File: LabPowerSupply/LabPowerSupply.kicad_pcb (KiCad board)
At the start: 4 copper layers, 213 parts, among them Q1_CP1 FMMT495TA, Q1_CP2 FMMT495TA, Q1_LVR1 PJA3404_R1_00001, Q1_LVR2 PJA3404_R1_00001, Q2_LVR1 PJA3404_R1_00001, Q2_LVR2 PJA3404_R1_00001, Q3_LVR1 PJA3404_R1_00001, Q3_LVR2 PJA3404_R1_00001, Y1 8M, Y2 8M

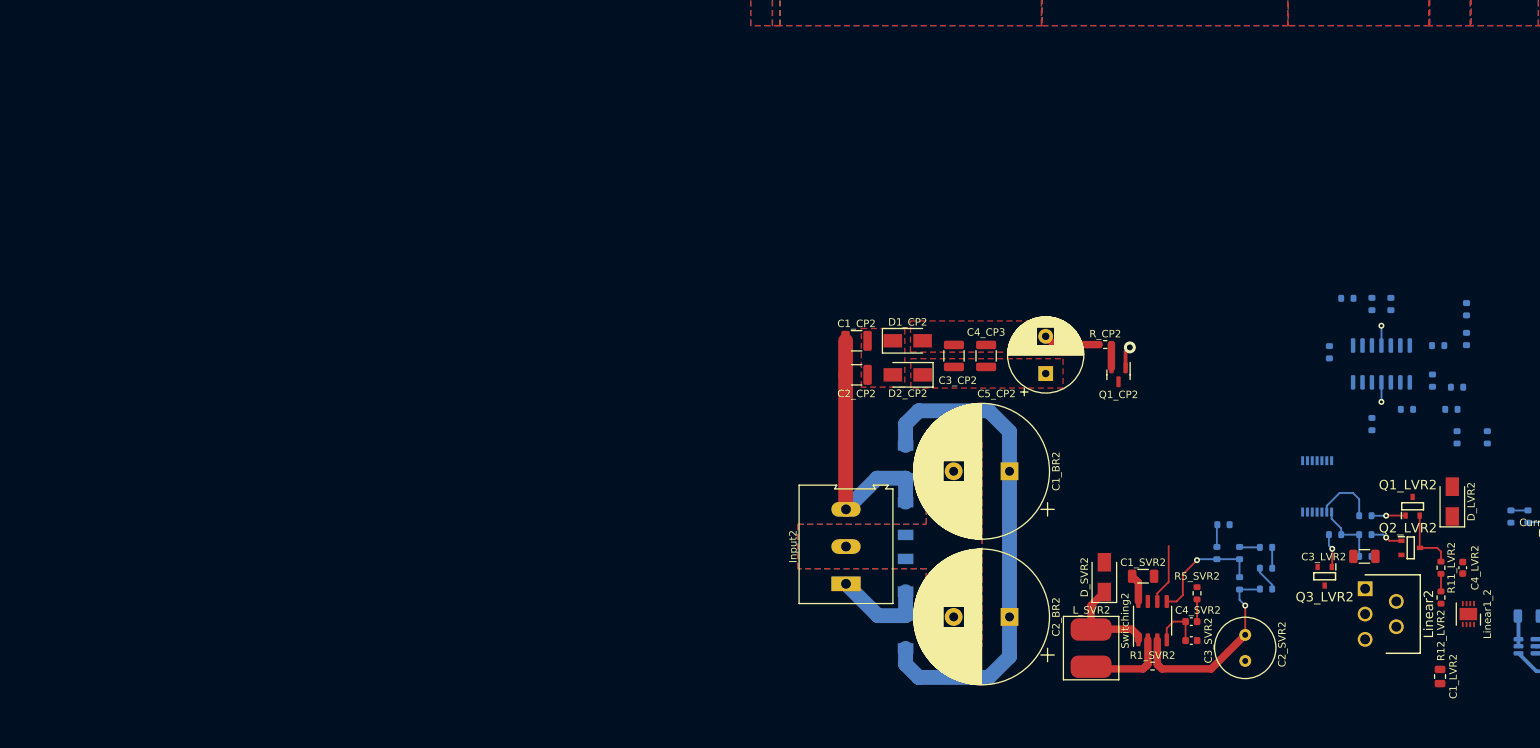
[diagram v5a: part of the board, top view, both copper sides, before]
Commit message: Began linear rework
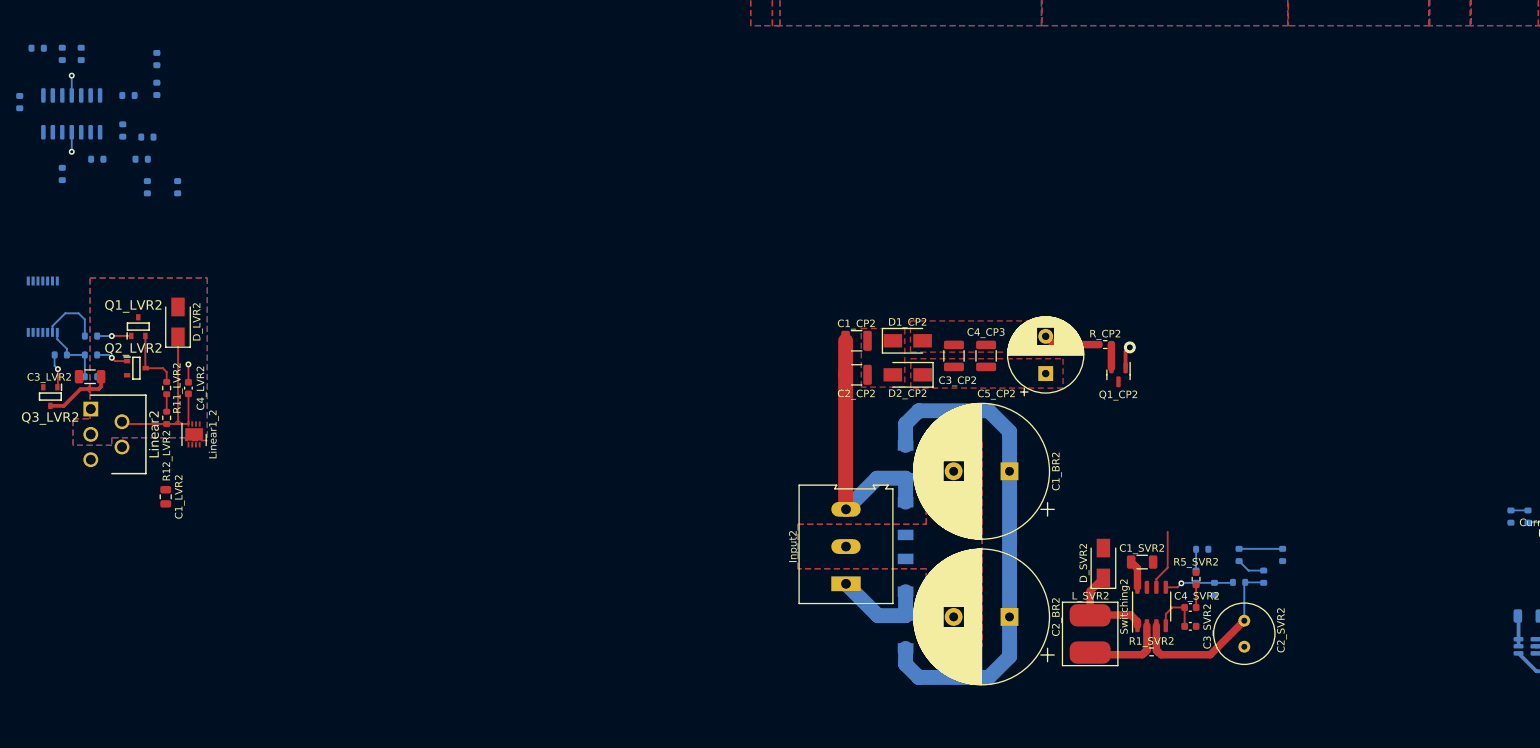
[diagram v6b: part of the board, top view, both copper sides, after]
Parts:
- moved R13_OA2 179.1 mm to (-80.4, 90.9)
- moved R2_OA2 179.1 mm to (-74.5, 91.6)
- moved R8_OA2 179.1 mm to (-65.7, 102.8)
- moved R91_OA2 179.1 mm to (-66.4, 105.8)
- moved R92_OA2 179.1 mm to (-65.7, 109.6)
- moved OpAmp2 179.1 mm to (-75.8, 99.7)
- moved R10_OA2 179.1 mm to (-61.6, 109.6)
- moved R11_OA2 179.1 mm to (-77.1, 107.8)
- moved R12_OA2 179.1 mm to (-77.1, 91.6)
- moved R3_OA2 179.1 mm to (-82.8, 98.1)
- moved R4_OA2 179.1 mm to (-69.0, 101.9)
- moved R51_OA2 179.1 mm to (-68.2, 97.2)
- moved R52_OA2 179.1 mm to (-64.4, 96.3)
- moved R6_OA2 179.1 mm to (-64.4, 92.3)
- moved R7_OA2 179.1 mm to (-72.4, 105.8)
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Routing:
- net Net-(C4_LVR2-Pad1): track 0.00 -> 24.8 mm
- net /Channel Power Supply 2/Charge Pump/Charge: track 5.90 -> 15.1 mm
- net /Channel Power Supply 2/Switching Voltage Regulator/FeedBack: track 16.2 -> 9.29 mm
- net /Channel Power Supply 2/ADC 1: track 2.79 -> 5.84 mm
- net /Channel Power Supply 2/Linear Voltage Regulator /Linear Input: track 26.5 -> 25.0 mm, vias 1 -> 0
- net GND2: track 5.74 -> 5.38 mm, vias 1 -> 2
- added copper zone on B.Cu, net /Channel Power Supply 2/Charge Pump/Charge
- added copper zone on F.Cu, net /Channel Power Supply 2/Charge Pump/Charge
- added copper zone on F.Cu, net Net-(C4_LVR2-Pad1)

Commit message: Ch2 restructure cont
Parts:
- moved R13_OA2 209.4 mm to (124.6, 133.6), turned to -90 degrees
- moved R2_OA2 207.4 mm to (127.7, 137.5), turned to 90 degrees
- moved R12_OA2 206.9 mm to (124.6, 137.5)
- moved R3_OA2 206.6 mm to (120.7, 133.7), turned to 180 degrees
- moved R11_OA2 200.3 mm to (119.0, 148.3)
- moved OpAmp2 199.2 mm to (119.2, 140.7), turned to 180 degrees
- moved R51_OA2 197.1 mm to (122.2, 148.3), turned to -90 degrees
- moved R6_OA2 196.8 mm to (125.8, 143.3), turned to 0 degrees
- moved R52_OA2 195.9 mm to (125.0, 146.6)
- moved R4_OA2 191.8 mm to (116.5, 150.9), turned to 90 degrees
- moved R7_OA2 189.9 mm to (113.6, 144.1), turned to -90 degrees
- moved R8_OA2 186.8 mm to (115.7, 147.6), turned to 180 degrees
- moved R91_OA2 178.8 mm to (108.2, 144.1), turned to 90 degrees
- moved R92_OA2 176.5 mm to (108.2, 140.1), turned to 90 degrees
- moved R10_OA2 175.0 mm to (110.7, 140.1), turned to -90 degrees
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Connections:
- Inverter2 pad 3: (no net) -> GND2
- Inverter2 pad 4: (no net) -> unconnected-(Inverter2-Pad4)
- Inverter2 pad 5: (no net) -> GND2
- Inverter2 pad 6: (no net) -> unconnected-(Inverter2-Pad6)
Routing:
- net /Channel Power Supply 2/Linear Voltage Regulator /Linear Input: track 25.0 -> 67.4 mm
- net /Channel Power Supply 2/Differential Op-Amp Circuit/Set Voltage: track 0.00 -> 24.0 mm, vias 0 -> 1
- net Net-(OpAmp2-Pad9): track 0.00 -> 21.0 mm
- net VDD: track 77.4 -> 97.6 mm, vias 1 -> 2
- net /Channel Power Supply 2/DAC 2: track 0.00 -> 16.7 mm
- net Net-(OpAmp2-Pad7): track 0.00 -> 16.7 mm
- net /Channel Power Supply 2/Current Sense /Output: track 25.0 -> 39.3 mm
- net Net-(OpAmp2-Pad10): track 0.00 -> 10.5 mm
- net Net-(OpAmp2-Pad12): track 0.00 -> 10.3 mm
- net GND2: track 5.38 -> 15.0 mm, vias 2 -> 4
- net Net-(OpAmp2-Pad3): track 0.00 -> 6.48 mm
- net Net-(OpAmp2-Pad6): track 0.00 -> 5.81 mm
- net /Channel Power Supply 2/Switching Voltage Regulator/FeedBack: track 9.29 -> 15.0 mm
- net Net-(OpAmp2-Pad1): track 0.00 -> 4.48 mm
- net Net-(R51_OA2-Pad2): track 0.00 -> 4.31 mm
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- added copper zone on F.Cu, net /Channel Power Supply 2/Linear Voltage Regulator /Linear Input
- added copper zone on F.Cu, net VDD

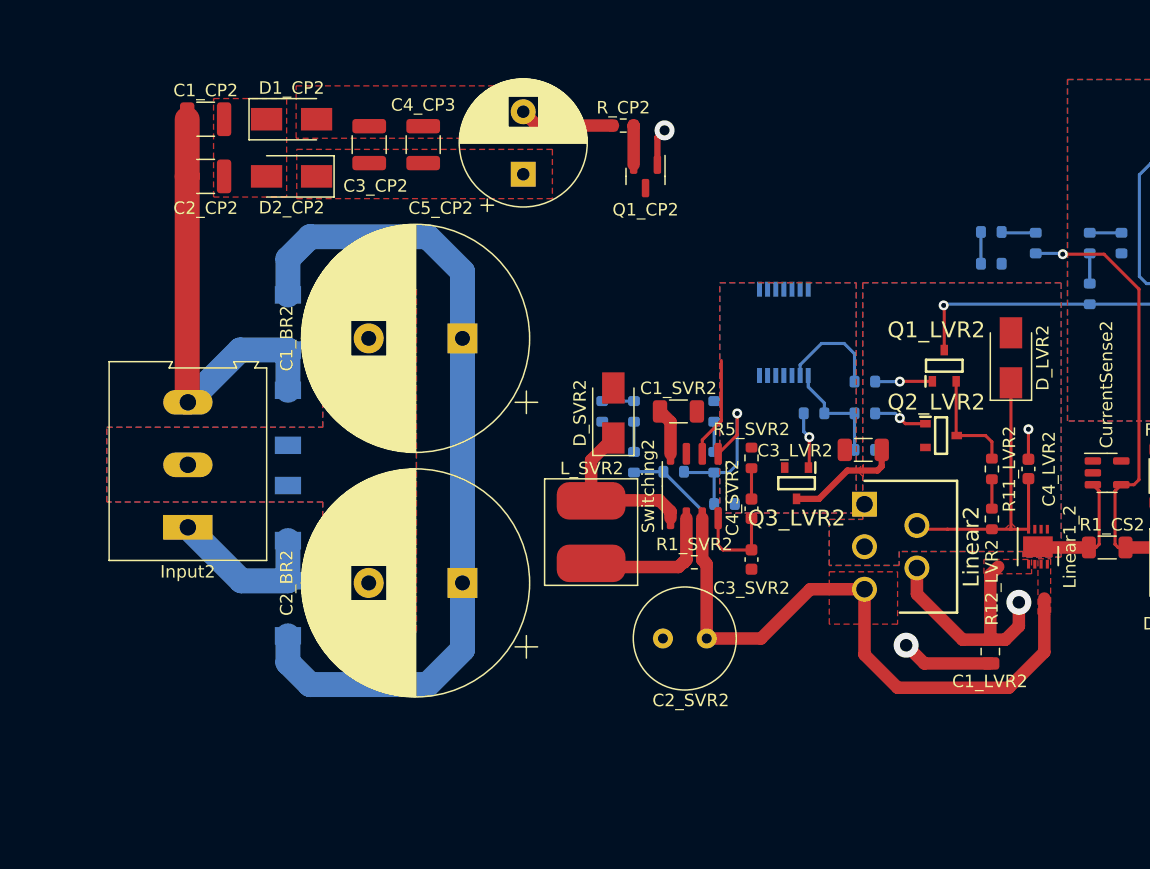
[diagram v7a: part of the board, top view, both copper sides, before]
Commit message: Moved charge pump
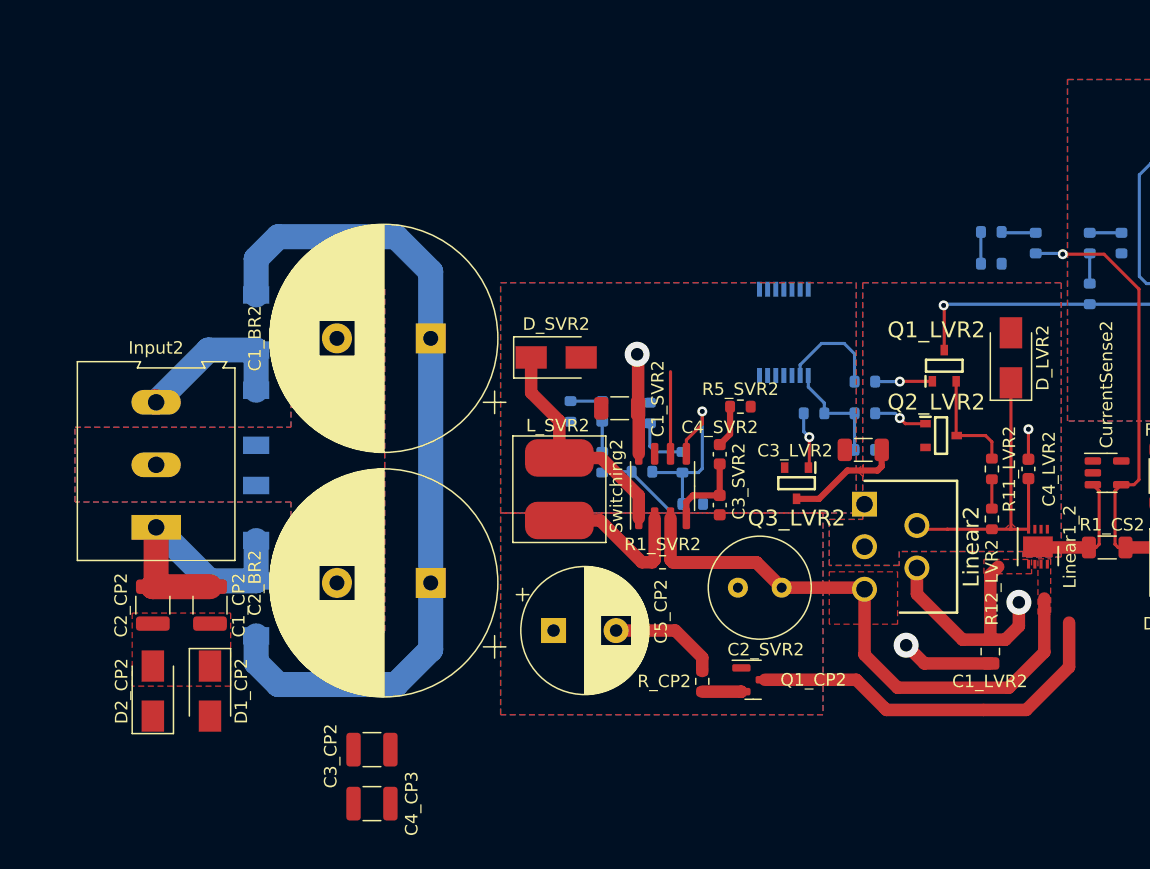
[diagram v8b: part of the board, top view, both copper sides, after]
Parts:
- moved C4_CP3 52.9 mm to (50.8, 184.9), turned to 180 degrees
- moved C3_CP2 48.4 mm to (50.8, 180.6), turned to 180 degrees
- moved D1_CP2 46.2 mm to (37.8, 175.9), turned to -90 degrees
- moved R_CP2 44.9 mm to (77.2, 175.1), turned to -90 degrees
- moved D2_CP2 42.6 mm to (33.3, 175.9), turned to 90 degrees
- moved Q1_CP2 41.2 mm to (81.3, 175.0), turned to 0 degrees
- moved C1_CP2 38.9 mm to (37.8, 169.0), turned to -90 degrees
- moved C5_CP2 36.6 mm to (65.3, 171.1), turned to 0 degrees
- moved C2_CP2 34.5 mm to (33.3, 169.0), turned to -90 degrees
- moved C2_SVR2 7.24 mm to (83.6, 167.6)
- moved D_SVR2 6.38 mm to (65.5, 149.2), turned to 0 degrees
- moved R41_SVR2 5.15 mm to (73.0, 153.7)
- moved C3_SVR2 5.04 mm to (78.6, 161.0)
- moved C4_SVR2 5.04 mm to (78.6, 157.0)
- moved C1_SVR2 4.71 mm to (70.6, 153.3), turned to 180 degrees
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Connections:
- C1_CP1 pad 1: /Channel Power Supply 1/AC 1 -> /Channel Power Supply 1/AC 2
- C1_CP2 pad 1: /Channel Power Supply 2/AC 1 -> /Channel Power Supply 2/AC 2
- C2_CP1 pad 1: /Channel Power Supply 1/AC 1 -> /Channel Power Supply 1/AC 2
- C2_CP2 pad 1: /Channel Power Supply 2/AC 1 -> /Channel Power Supply 2/AC 2
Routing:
- net /Channel Power Supply 2/Charge Pump/Charge: track 19.2 -> 49.5 mm
- net /Channel Power Supply 2/AC 1: track 36.6 -> 13.0 mm
- net /Channel Power Supply 2/AC 2: track 13.0 -> 22.4 mm
- net /Channel Power Supply 2/Linear Voltage Regulator /Linear Input: track 67.4 -> 75.7 mm
- net Net-(D_SVR2-Pad1): track 13.0 -> 18.4 mm
- net VDD: track 97.6 -> 101.9 mm, vias 2 -> 3
- net GND2: track 15.0 -> 12.0 mm, vias 4 -> 3
- net Net-(R41_SVR2-Pad1): track 2.41 -> 4.63 mm
- net /Channel Power Supply 2/Differential Op-Amp Circuit/3.3 Volts: track 8.09 -> 6.57 mm
- net Net-(C1_CP2-Pad2): track 1.43 -> 0.00 mm
- net /Channel Power Supply 2/Charge Pump/Negative: track 10.3 -> 11.5 mm
- net Net-(L_SVR2-Pad2): track 11.4 -> 12.4 mm
- net Net-(C4_SVR2-Pad2): track 2.46 -> 3.38 mm
- net Net-(C3_SVR2-Pad1): track 7.50 -> 6.70 mm
- removed copper zone on F.Cu, net /Channel Power Supply 2/Charge Pump/Negative
